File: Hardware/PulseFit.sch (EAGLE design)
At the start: 49 parts, among them SW1 SWITCH.JS202011JCQN

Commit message: first itteration of pulsefit
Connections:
- net PEAK: now also BREAKOUT.3; no longer BREAKOUT.2
- net PULSE: now also BREAKOUT.2; no longer BREAKOUT.3
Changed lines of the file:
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@@
 <?xml version="1.0" encoding="utf-8"?>
 <!DOCTYPE eagle SYSTEM "eagle.dtd">
-<eagle version="8.2.1">
+<eagle version="8.0.0">
 <drawing>
 <settings>
@@
 </segment>
 <segment>
-<pinref part="BREAKOUT" gate="G$1" pin="3"/>
-<wire x1="236.22" y1="22.86" x2="238.76" y2="22.86" width="0.1524" layer="91"/>
-<label x="238.76" y="22.86" size="1.27" layer="95" xref="yes"/>
+<pinref part="BREAKOUT" gate="G$1" pin="2"/>
+<wire x1="236.22" y1="20.32" x2="238.76" y2="20.32" width="0.1524" layer="91"/>
+<label x="238.76" y="20.32" size="1.27" layer="95" xref="yes"/>
 </segment>
 </net>
@@
 </segment>
 <segment>
-<pinref part="BREAKOUT" gate="G$1" pin="2"/>
-<wire x1="236.22" y1="20.32" x2="238.76" y2="20.32" width="0.1524" layer="91"/>
-<label x="238.76" y="20.32" size="1.27" layer="95" xref="yes"/>
+<pinref part="BREAKOUT" gate="G$1" pin="3"/>
+<wire x1="236.22" y1="22.86" x2="238.76" y2="22.86" width="0.1524" layer="91"/>
+<label x="238.76" y="22.86" size="1.27" layer="95" xref="yes"/>
 </segment>
 </net>

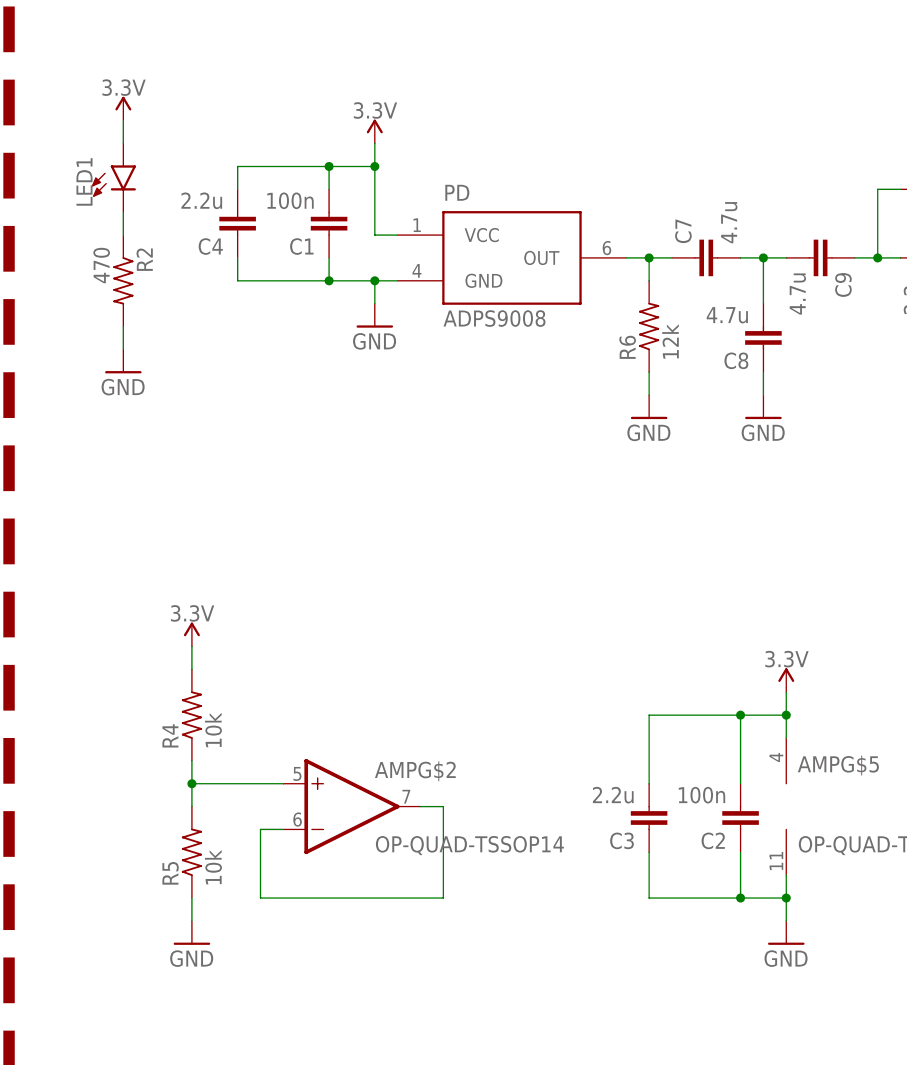
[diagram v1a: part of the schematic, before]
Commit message: deleted extra bypass capacitors and changed their values a bit
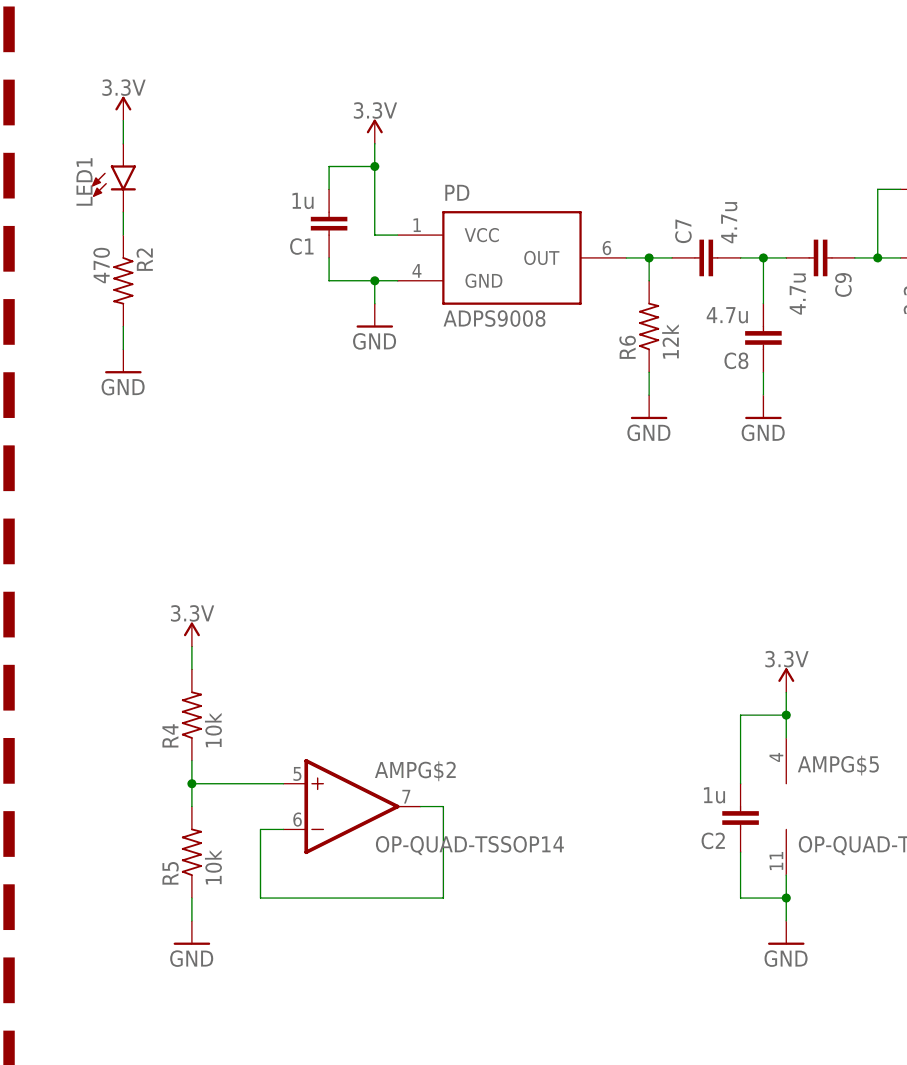
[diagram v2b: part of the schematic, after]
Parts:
- removed C3, C4: 2.2u, CalvEngIO-Passives:CAPACITOR0603
- C1, C2: value 100n -> 1u
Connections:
- net 3.3V: no longer C3.2, C4.2
- net GND: no longer C3.1, C4.1
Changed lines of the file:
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@@
 <?xml version="1.0" encoding="utf-8"?>
 <!DOCTYPE eagle SYSTEM "eagle.dtd">
-<eagle version="8.0.0">
+<eagle version="8.2.2">
 <drawing>
 <settings>
@@
 <part name="GND9" library="SparkFun-Aesthetics" deviceset="GND" device=""/>
 <part name="GND11" library="SparkFun-Aesthetics" deviceset="GND" device=""/>
-<part name="C2" library="CalvEngIO-Passives" deviceset="CAPACITOR" device="0402" value="100n"/>
+<part name="C2" library="CalvEngIO-Passives" deviceset="CAPACITOR" device="0402" value="1u"/>
 <part name="BREAKOUT" library="CalvEngIO-Connectors" deviceset="CONN_05" device=""/>
 <part name="GND13" library="SparkFun-Aesthetics" deviceset="GND" device=""/>
@@
 <part name="GND24" library="SparkFun-Aesthetics" deviceset="GND" device=""/>
 <part name="GND25" library="SparkFun-Aesthetics" deviceset="GND" device=""/>
-<part name="C1" library="CalvEngIO-Passives" deviceset="CAPACITOR" device="0402" value="100n"/>
+<part name="C1" library="CalvEngIO-Passives" deviceset="CAPACITOR" device="0402" value="1u"/>
 <part name="R5" library="CalvEngIO-Passives" deviceset="RESISTOR" device="0402" value="10k"/>
 <part name="R4" library="CalvEngIO-Passives" deviceset="RESISTOR" device="0402" value="10k"/>
@@
 <part name="D1" library="CalvEngIO-DiscreteSemi" deviceset="SCHOTTKY" device="-SOD-123FL"/>
 <part name="AMP" library="CalvEngIO-AnalogIC" deviceset="OP-QUAD" device="-TSSOP14" value="OP-QUAD-TSSOP14"/>
-<part name="C3" library="CalvEngIO-Passives" deviceset="CAPACITOR" device="0603" value="2.2u"/>
-<part name="C4" library="CalvEngIO-Passives" deviceset="CAPACITOR" device="0603" value="2.2u"/>
 <part name="U$6" library="CalvEngIO-Power" deviceset="AP2210-ADJ" device=""/>
 <part name="GND3" library="SparkFun-Aesthetics" deviceset="GND" device=""/>
@@
 <instance part="AMP" gate="G$4" x="198.12" y="96.52"/>
 <instance part="AMP" gate="G$5" x="81.28" y="17.78"/>
-<instance part="C3" gate="G$1" x="66.04" y="17.78" rot="R180"/>
-<instance part="C4" gate="G$1" x="20.32" y="83.82" rot="R180"/>
 <instance part="U$6" gate="G$1" x="180.34" y="22.86"/>
 <instance part="GND3" gate="1" x="160.02" y="12.7"/>
@@
 <junction x="81.28" y="7.62"/>
 <pinref part="AMP" gate="G$5" pin="V-"/>
-<pinref part="C3" gate="G$1" pin="1"/>
-<wire x1="66.04" y1="12.7" x2="66.04" y2="7.62" width="0.1524" layer="91"/>
-<wire x1="66.04" y1="7.62" x2="76.2" y2="7.62" width="0.1524" layer="91"/>
-<junction x="76.2" y="7.62"/>
 </segment>
 <segment>
@@
 <wire x1="30.48" y1="76.2" x2="35.56" y2="76.2" width="0.1524" layer="91"/>
 <junction x="35.56" y="76.2"/>
-<pinref part="C4" gate="G$1" pin="1"/>
-<wire x1="20.32" y1="78.74" x2="20.32" y2="76.2" width="0.1524" layer="91"/>
-<wire x1="20.32" y1="76.2" x2="30.48" y2="76.2" width="0.1524" layer="91"/>
-<junction x="30.48" y="76.2"/>
 </segment>
 <segment>
@@
 <junction x="81.28" y="27.94"/>
 <pinref part="AMP" gate="G$5" pin="V+"/>
-<pinref part="C3" gate="G$1" pin="2"/>
-<wire x1="66.04" y1="20.32" x2="66.04" y2="27.94" width="0.1524" layer="91"/>
-<wire x1="66.04" y1="27.94" x2="76.2" y2="27.94" width="0.1524" layer="91"/>
-<junction x="76.2" y="27.94"/>
 <pinref part="SUPPLY4" gate="G$1" pin="3.3V"/>
 </segment>
@@
 <wire x1="30.48" y1="88.9" x2="35.56" y2="88.9" width="0.1524" layer="91"/>
 <junction x="35.56" y="88.9"/>
-<pinref part="C4" gate="G$1" pin="2"/>
-<wire x1="20.32" y1="86.36" x2="20.32" y2="88.9" width="0.1524" layer="91"/>
-<wire x1="20.32" y1="88.9" x2="30.48" y2="88.9" width="0.1524" layer="91"/>
-<junction x="30.48" y="88.9"/>
 <pinref part="SUPPLY7" gate="G$1" pin="3.3V"/>
 </segment>

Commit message: slight updates moving capacitors around and such
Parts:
- added U$1: CALVENGIO_HANDLEHANDLE.08, CalvEngIO-Logos:CALVENGIO_HANDLEHANDLE.08
- D1: device CalvEngIO-DiscreteSemi:SCHOTTKY-SOD-123FL -> CalvEngIO-DiscreteSemi:DIODE-BAS16J
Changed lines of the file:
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@@
 <part name="SW1" library="CalvEngIO-Switches" deviceset="SWITCH.JS202011JCQN" device=""/>
 <part name="GND2" library="SparkFun-Aesthetics" deviceset="GND" device=""/>
-<part name="D1" library="CalvEngIO-DiscreteSemi" deviceset="SCHOTTKY" device="-SOD-123FL"/>
+<part name="D1" library="CalvEngIO-DiscreteSemi" deviceset="DIODE" device="-BAS16J"/>
 <part name="AMP" library="CalvEngIO-AnalogIC" deviceset="OP-QUAD" device="-TSSOP14" value="OP-QUAD-TSSOP14"/>
 <part name="U$6" library="CalvEngIO-Power" deviceset="AP2210-ADJ" device=""/>
@@
 <part name="SUPPLY6" library="CalvEngIO-Symbols" deviceset="3.3V" device=""/>
 <part name="SUPPLY7" library="CalvEngIO-Symbols" deviceset="3.3V" device=""/>
+<part name="U$1" library="CalvEngIO-Logos" deviceset="CALVENGIO_HANDLE" device="HANDLE.08"/>
 </parts>
 <sheets>
@@
 <instance part="SUPPLY6" gate="G$1" x="7.62" y="93.98"/>
 <instance part="SUPPLY7" gate="G$1" x="35.56" y="91.44"/>
+<instance part="U$1" gate="G$1" x="203.2" y="-15.24"/>
 </instances>
 <busses>
